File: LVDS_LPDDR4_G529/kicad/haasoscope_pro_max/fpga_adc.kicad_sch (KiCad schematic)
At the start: 2 parts, among them IC1 ADC12DL500ACF_Aligned, U3 Ti90G529_Functions

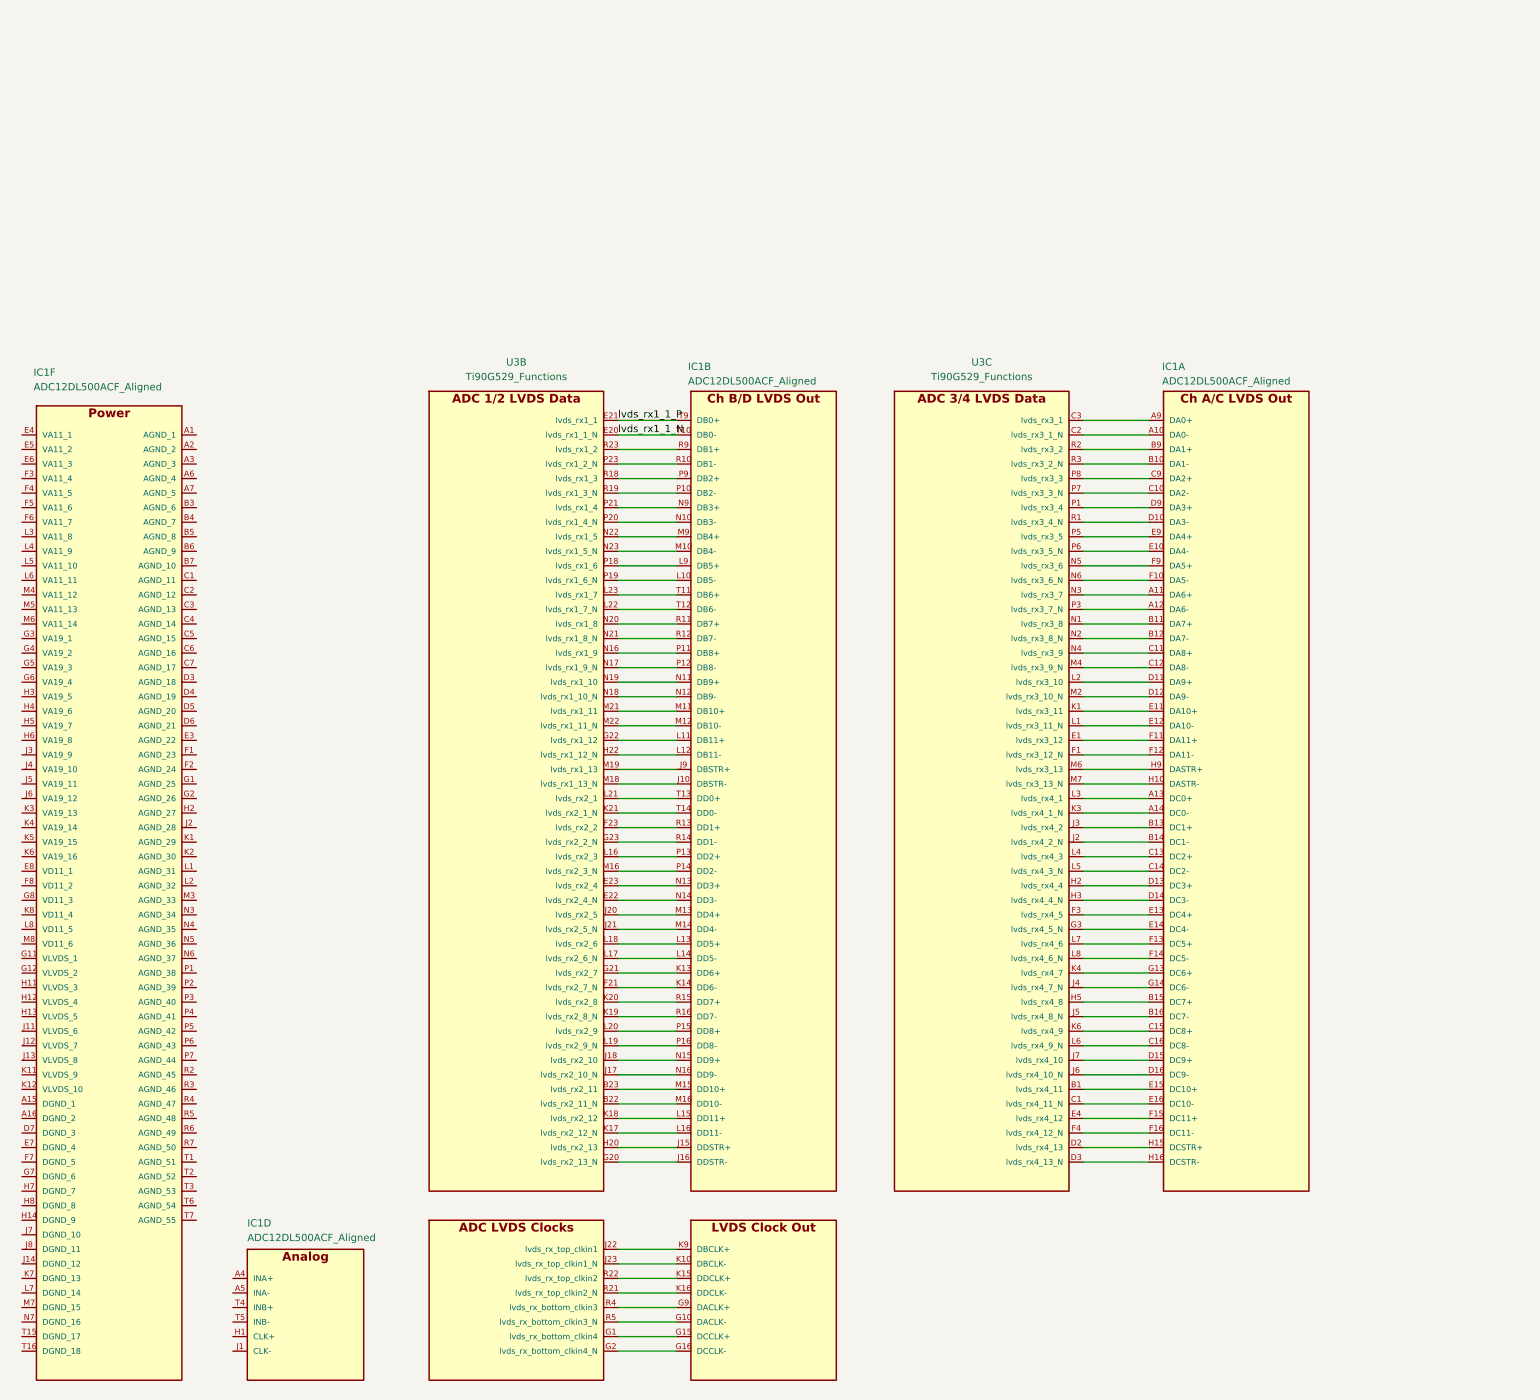
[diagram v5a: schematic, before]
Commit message: 6 NC pads
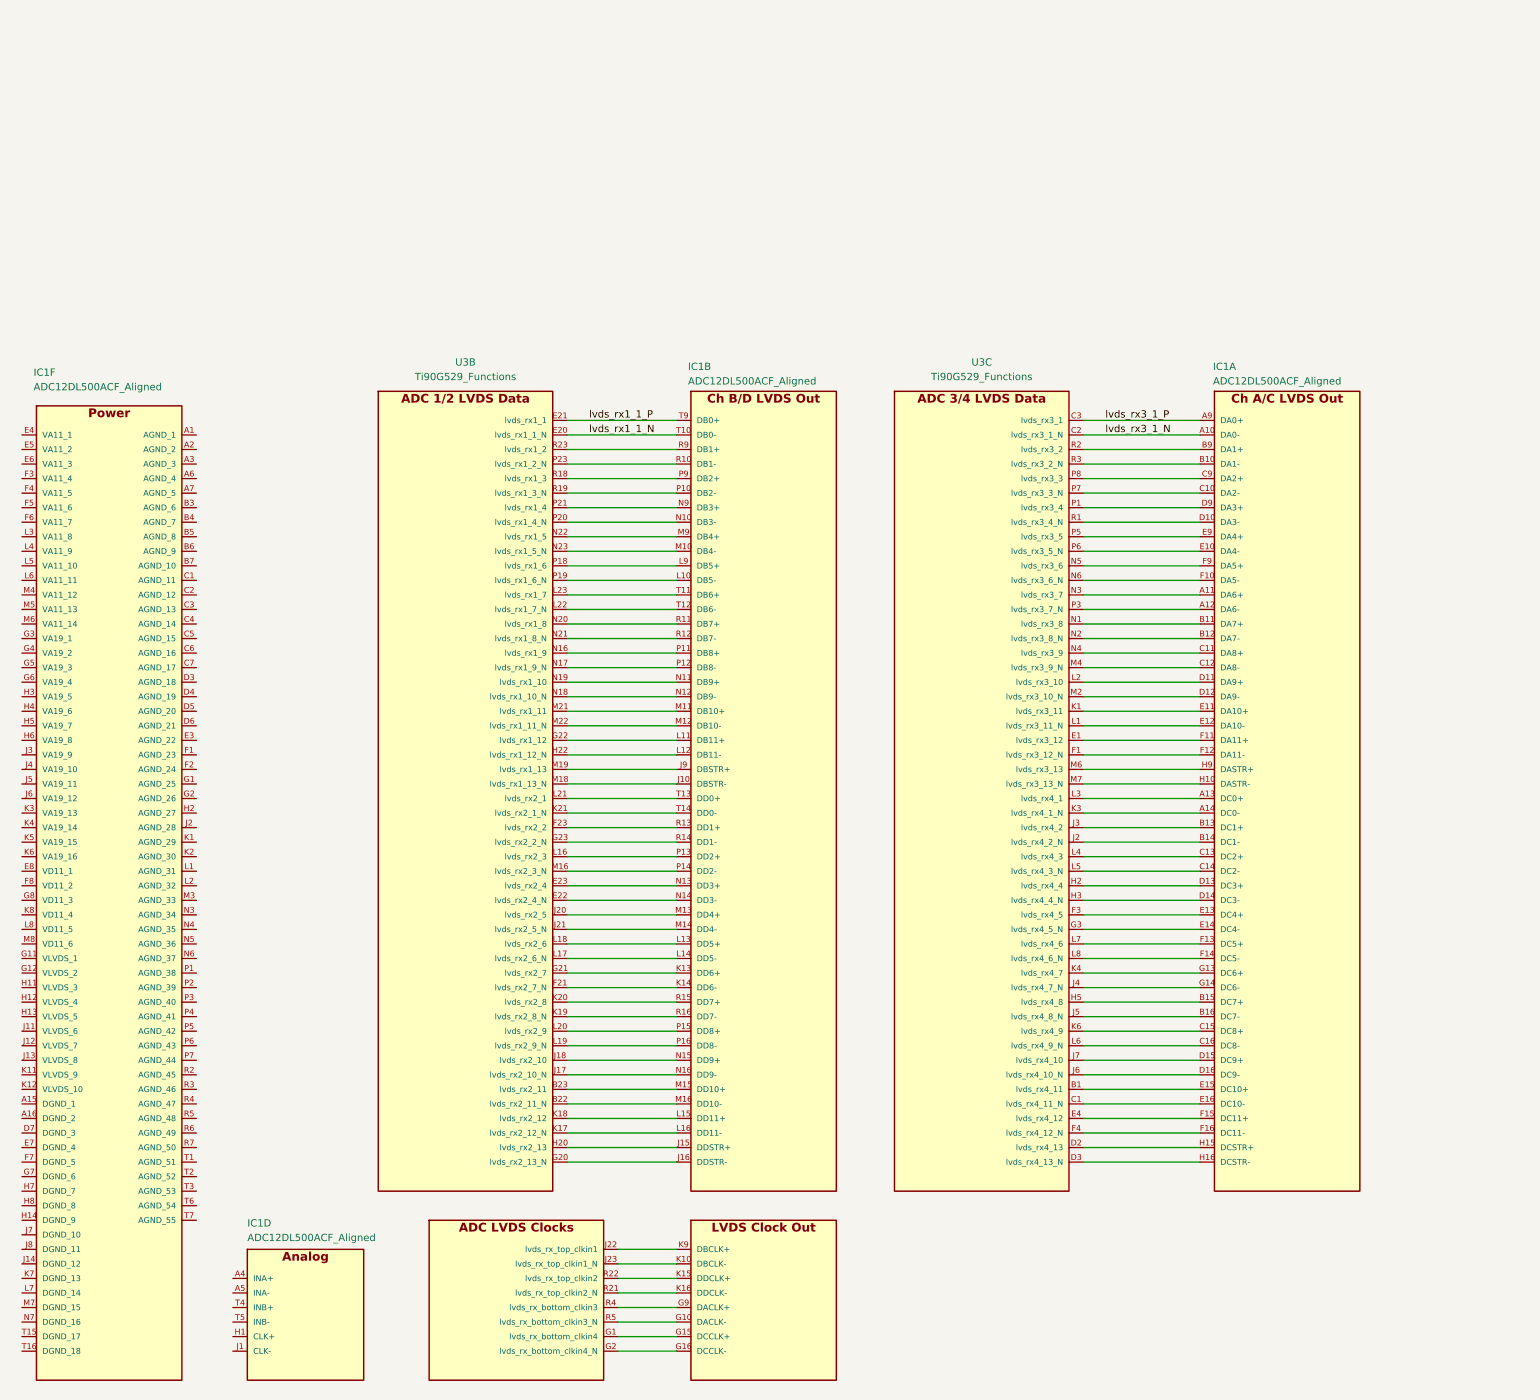
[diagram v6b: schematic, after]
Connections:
- net lvds_rx3_1_N: now reaches IC1.A10 (DA0-), U3.C2 (lvds_rx3_1_N)
- net lvds_rx3_1_P: now reaches IC1.A9 (DA0+), U3.C3 (lvds_rx3_1)
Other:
- moved on the sheet: IC1A, U3B

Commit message: add labels for all lvds_rx nets
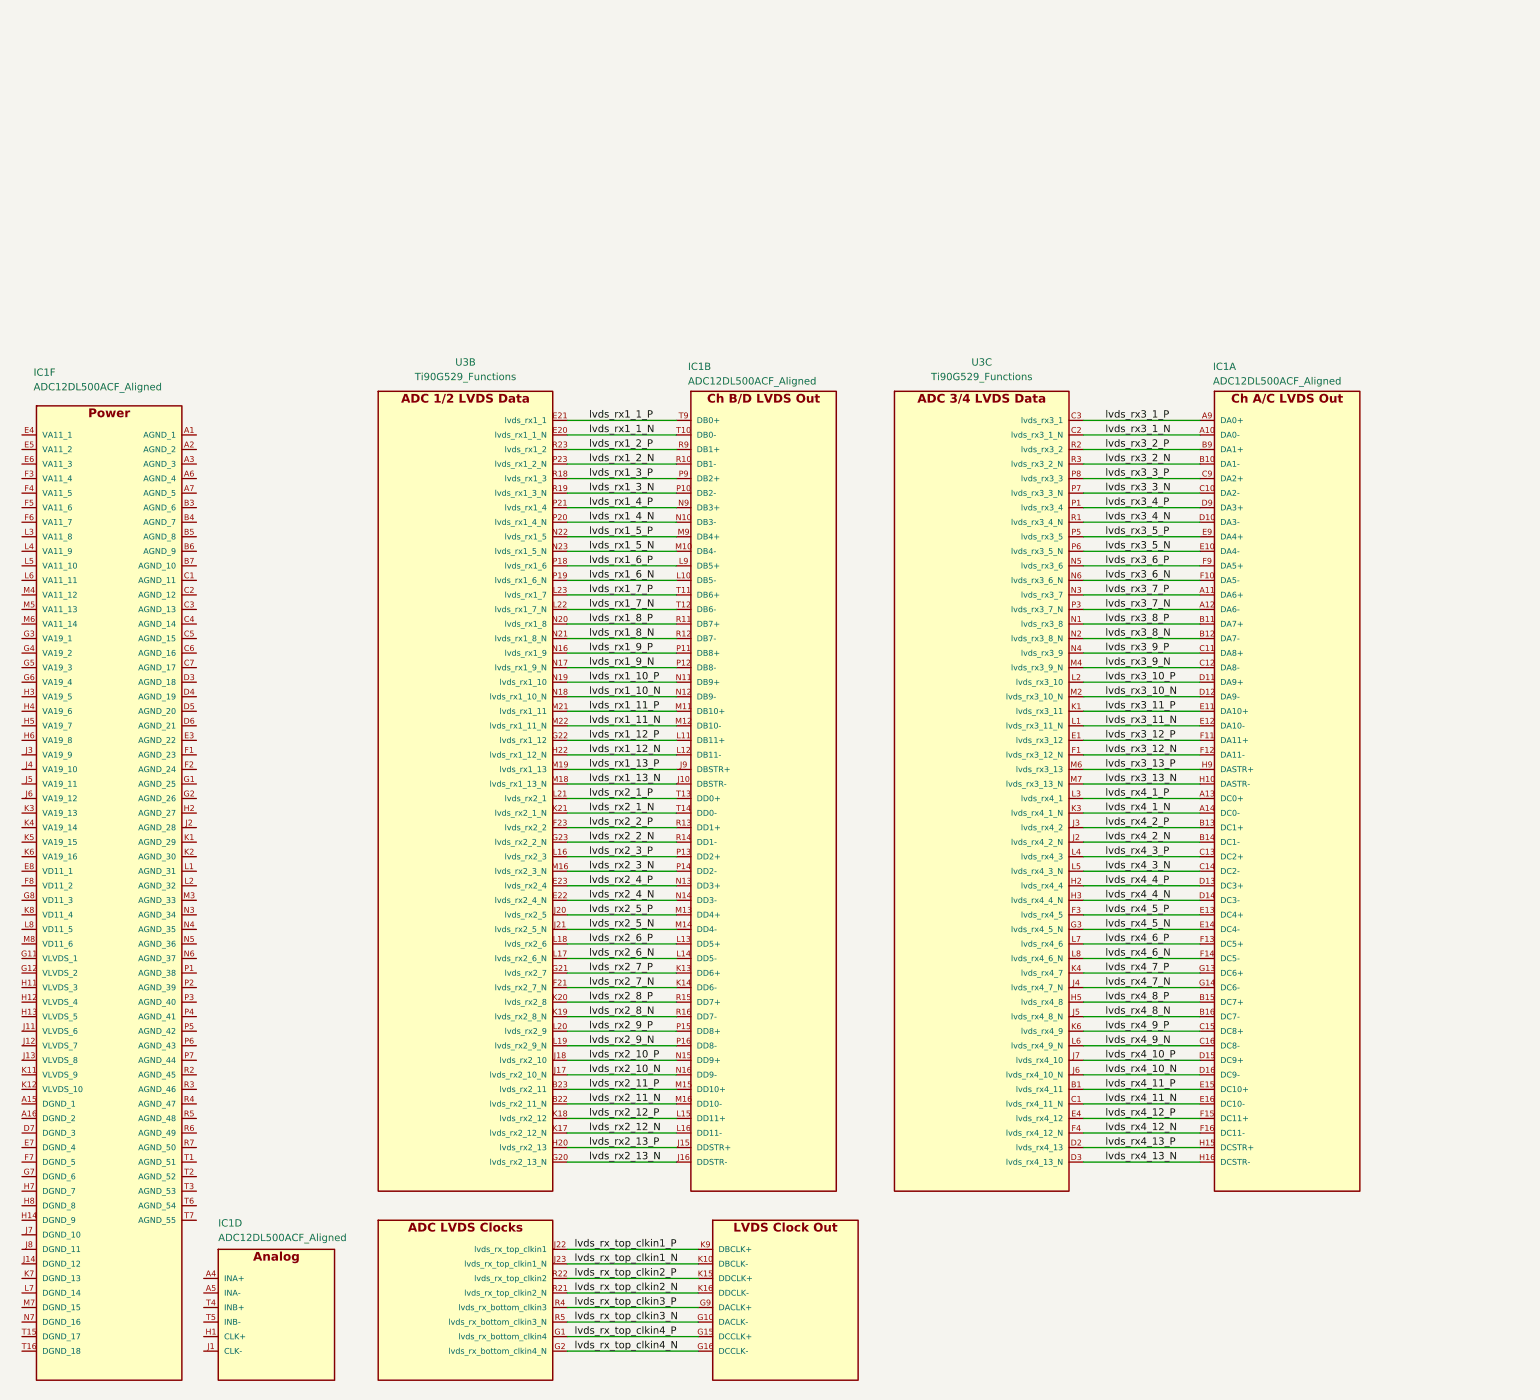
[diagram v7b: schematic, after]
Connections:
- net lvds_rx4_11_P: now reaches IC1.E15 (DC10+), U3.B1 (lvds_rx4_11)
- net lvds_rx4_11_N: now reaches IC1.E16 (DC10-), U3.C1 (lvds_rx4_11_N)
- net lvds_rx4_13_P: now reaches IC1.H15 (DCSTR+), U3.D2 (lvds_rx4_13)
- net lvds_rx4_13_N: now reaches IC1.H16 (DCSTR-), U3.D3 (lvds_rx4_13_N)
- net lvds_rx3_12_P: now reaches IC1.F11 (DA11+), U3.E1 (lvds_rx3_12)
- net lvds_rx4_12_P: now reaches IC1.F15 (DC11+), U3.E4 (lvds_rx4_12)
- net lvds_rx3_12_N: now reaches IC1.F12 (DA11-), U3.F1 (lvds_rx3_12_N)
- net lvds_rx4_5_P: now reaches IC1.E13 (DC4+), U3.F3 (lvds_rx4_5)
- net lvds_rx4_12_N: now reaches IC1.F16 (DC11-), U3.F4 (lvds_rx4_12_N)
- net lvds_rx4_5_N: now reaches IC1.E14 (DC4-), U3.G3 (lvds_rx4_5_N)
- net lvds_rx4_4_P: now reaches IC1.D13 (DC3+), U3.H2 (lvds_rx4_4)
- net lvds_rx4_4_N: now reaches IC1.D14 (DC3-), U3.H3 (lvds_rx4_4_N)
- net lvds_rx4_8_P: now reaches IC1.B15 (DC7+), U3.H5 (lvds_rx4_8)
- net lvds_rx4_2_N: now reaches IC1.B14 (DC1-), U3.J2 (lvds_rx4_2_N)
- net lvds_rx4_2_P: now reaches IC1.B13 (DC1+), U3.J3 (lvds_rx4_2)
- net lvds_rx4_7_N: now reaches IC1.G14 (DC6-), U3.J4 (lvds_rx4_7_N)
- net lvds_rx4_8_N: now reaches IC1.B16 (DC7-), U3.J5 (lvds_rx4_8_N)
- net lvds_rx4_10_N: now reaches IC1.D16 (DC9-), U3.J6 (lvds_rx4_10_N)
- net lvds_rx4_10_P: now reaches IC1.D15 (DC9+), U3.J7 (lvds_rx4_10)
- net lvds_rx3_11_P: now reaches IC1.E11 (DA10+), U3.K1 (lvds_rx3_11)
- net lvds_rx4_1_N: now reaches IC1.A14 (DC0-), U3.K3 (lvds_rx4_1_N)
- net lvds_rx4_7_P: now reaches IC1.G13 (DC6+), U3.K4 (lvds_rx4_7)
- net lvds_rx4_9_P: now reaches IC1.C15 (DC8+), U3.K6 (lvds_rx4_9)
- net lvds_rx3_11_N: now reaches IC1.E12 (DA10-), U3.L1 (lvds_rx3_11_N)
- net lvds_rx3_10_P: now reaches IC1.D11 (DA9+), U3.L2 (lvds_rx3_10)
- net lvds_rx4_1_P: now reaches IC1.A13 (DC0+), U3.L3 (lvds_rx4_1)
- net lvds_rx4_3_P: now reaches IC1.C13 (DC2+), U3.L4 (lvds_rx4_3)
- net lvds_rx4_3_N: now reaches IC1.C14 (DC2-), U3.L5 (lvds_rx4_3_N)
- net lvds_rx4_9_N: now reaches IC1.C16 (DC8-), U3.L6 (lvds_rx4_9_N)
- net lvds_rx4_6_P: now reaches IC1.F13 (DC5+), U3.L7 (lvds_rx4_6)
- net lvds_rx4_6_N: now reaches IC1.F14 (DC5-), U3.L8 (lvds_rx4_6_N)
- net lvds_rx3_10_N: now reaches IC1.D12 (DA9-), U3.M2 (lvds_rx3_10_N)
- net lvds_rx3_9_N: now reaches IC1.C12 (DA8-), U3.M4 (lvds_rx3_9_N)
- net lvds_rx3_13_P: now reaches IC1.H9 (DASTR+), U3.M6 (lvds_rx3_13)
- net lvds_rx3_13_N: now reaches IC1.H10 (DASTR-), U3.M7 (lvds_rx3_13_N)
- net lvds_rx3_8_P: now reaches IC1.B11 (DA7+), U3.N1 (lvds_rx3_8)
- net lvds_rx3_8_N: now reaches IC1.B12 (DA7-), U3.N2 (lvds_rx3_8_N)
- net lvds_rx3_7_P: now reaches IC1.A11 (DA6+), U3.N3 (lvds_rx3_7)
- net lvds_rx3_9_P: now reaches IC1.C11 (DA8+), U3.N4 (lvds_rx3_9)
- net lvds_rx3_6_P: now reaches IC1.F9 (DA5+), U3.N5 (lvds_rx3_6)
- net lvds_rx3_6_N: now reaches IC1.F10 (DA5-), U3.N6 (lvds_rx3_6_N)
- net lvds_rx3_4_P: now reaches IC1.D9 (DA3+), U3.P1 (lvds_rx3_4)
- net lvds_rx3_7_N: now reaches IC1.A12 (DA6-), U3.P3 (lvds_rx3_7_N)
- net lvds_rx3_5_P: now reaches IC1.E9 (DA4+), U3.P5 (lvds_rx3_5)
- net lvds_rx3_5_N: now reaches IC1.E10 (DA4-), U3.P6 (lvds_rx3_5_N)
- net lvds_rx3_3_N: now reaches IC1.C10 (DA2-), U3.P7 (lvds_rx3_3_N)
- net lvds_rx3_3_P: now reaches IC1.C9 (DA2+), U3.P8 (lvds_rx3_3)
- net lvds_rx3_4_N: now reaches IC1.D10 (DA3-), U3.R1 (lvds_rx3_4_N)
- net lvds_rx3_2_P: now reaches IC1.B9 (DA1+), U3.R2 (lvds_rx3_2)
- net lvds_rx3_2_N: now reaches IC1.B10 (DA1-), U3.R3 (lvds_rx3_2_N)
- net lvds_rx2_11_N: now reaches IC1.M16 (DD10-), U3.B22 (lvds_rx2_11_N)
- net lvds_rx2_11_P: now reaches IC1.M15 (DD10+), U3.B23 (lvds_rx2_11)
- net lvds_rx2_4_N: now reaches IC1.N14 (DD3-), U3.E22 (lvds_rx2_4_N)
- net lvds_rx2_4_P: now reaches IC1.N13 (DD3+), U3.E23 (lvds_rx2_4)
- net lvds_rx2_7_N: now reaches IC1.K14 (DD6-), U3.F21 (lvds_rx2_7_N)
- net lvds_rx2_2_P: now reaches IC1.R13 (DD1+), U3.F23 (lvds_rx2_2)
- net lvds_rx2_13_N: now reaches IC1.J16 (DDSTR-), U3.G20 (lvds_rx2_13_N)
- net lvds_rx2_7_P: now reaches IC1.K13 (DD6+), U3.G21 (lvds_rx2_7)
- net lvds_rx1_12_P: now reaches IC1.L11 (DB11+), U3.G22 (lvds_rx1_12)
- net lvds_rx2_2_N: now reaches IC1.R14 (DD1-), U3.G23 (lvds_rx2_2_N)
- net lvds_rx2_13_P: now reaches IC1.J15 (DDSTR+), U3.H20 (lvds_rx2_13)
- net lvds_rx1_12_N: now reaches IC1.L12 (DB11-), U3.H22 (lvds_rx1_12_N)
- net lvds_rx2_10_N: now reaches IC1.N16 (DD9-), U3.J17 (lvds_rx2_10_N)
- net lvds_rx2_10_P: now reaches IC1.N15 (DD9+), U3.J18 (lvds_rx2_10)
- net lvds_rx2_5_P: now reaches IC1.M13 (DD4+), U3.J20 (lvds_rx2_5)
- net lvds_rx2_5_N: now reaches IC1.M14 (DD4-), U3.J21 (lvds_rx2_5_N)
- net lvds_rx2_12_N: now reaches IC1.L16 (DD11-), U3.K17 (lvds_rx2_12_N)
- net lvds_rx2_12_P: now reaches IC1.L15 (DD11+), U3.K18 (lvds_rx2_12)
- net lvds_rx2_8_N: now reaches IC1.R16 (DD7-), U3.K19 (lvds_rx2_8_N)
- net lvds_rx2_8_P: now reaches IC1.R15 (DD7+), U3.K20 (lvds_rx2_8)
- net lvds_rx2_1_N: now reaches IC1.T14 (DD0-), U3.K21 (lvds_rx2_1_N)
- net lvds_rx2_3_P: now reaches IC1.P13 (DD2+), U3.L16 (lvds_rx2_3)
- net lvds_rx2_6_N: now reaches IC1.L14 (DD5-), U3.L17 (lvds_rx2_6_N)
- net lvds_rx2_6_P: now reaches IC1.L13 (DD5+), U3.L18 (lvds_rx2_6)
- net lvds_rx2_9_N: now reaches IC1.P16 (DD8-), U3.L19 (lvds_rx2_9_N)
- net lvds_rx2_9_P: now reaches IC1.P15 (DD8+), U3.L20 (lvds_rx2_9)
- net lvds_rx2_1_P: now reaches IC1.T13 (DD0+), U3.L21 (lvds_rx2_1)
- net lvds_rx1_7_N: now reaches IC1.T12 (DB6-), U3.L22 (lvds_rx1_7_N)
- net lvds_rx1_7_P: now reaches IC1.T11 (DB6+), U3.L23 (lvds_rx1_7)
- net lvds_rx2_3_N: now reaches IC1.P14 (DD2-), U3.M16 (lvds_rx2_3_N)
- net lvds_rx1_13_N: now reaches IC1.J10 (DBSTR-), U3.M18 (lvds_rx1_13_N)
- net lvds_rx1_13_P: now reaches IC1.J9 (DBSTR+), U3.M19 (lvds_rx1_13)
- net lvds_rx1_11_P: now reaches IC1.M11 (DB10+), U3.M21 (lvds_rx1_11)
- net lvds_rx1_11_N: now reaches IC1.M12 (DB10-), U3.M22 (lvds_rx1_11_N)
- net lvds_rx1_9_P: now reaches IC1.P11 (DB8+), U3.N16 (lvds_rx1_9)
- net lvds_rx1_9_N: now reaches IC1.P12 (DB8-), U3.N17 (lvds_rx1_9_N)
- net lvds_rx1_10_N: now reaches IC1.N12 (DB9-), U3.N18 (lvds_rx1_10_N)
- net lvds_rx1_10_P: now reaches IC1.N11 (DB9+), U3.N19 (lvds_rx1_10)
- net lvds_rx1_8_P: now reaches IC1.R11 (DB7+), U3.N20 (lvds_rx1_8)
- net lvds_rx1_8_N: now reaches IC1.R12 (DB7-), U3.N21 (lvds_rx1_8_N)
- net lvds_rx1_5_P: now reaches IC1.M9 (DB4+), U3.N22 (lvds_rx1_5)
- net lvds_rx1_5_N: now reaches IC1.M10 (DB4-), U3.N23 (lvds_rx1_5_N)
- net lvds_rx1_6_P: now reaches IC1.L9 (DB5+), U3.P18 (lvds_rx1_6)
- net lvds_rx1_6_N: now reaches IC1.L10 (DB5-), U3.P19 (lvds_rx1_6_N)
- net lvds_rx1_4_N: now reaches IC1.N10 (DB3-), U3.P20 (lvds_rx1_4_N)
- net lvds_rx1_4_P: now reaches IC1.N9 (DB3+), U3.P21 (lvds_rx1_4)
- net lvds_rx1_2_N: now reaches IC1.R10 (DB1-), U3.P23 (lvds_rx1_2_N)
- net lvds_rx1_3_P: now reaches IC1.P9 (DB2+), U3.R18 (lvds_rx1_3)
- net lvds_rx1_3_N: now reaches IC1.P10 (DB2-), U3.R19 (lvds_rx1_3_N)
- net lvds_rx1_2_P: now reaches IC1.R9 (DB1+), U3.R23 (lvds_rx1_2)
- net lvds_rx_top_clkin4_P: now reaches IC1.G15 (DCCLK+), U3.G1 (lvds_rx_bottom_clkin4)
- net lvds_rx_top_clkin4_N: now reaches IC1.G16 (DCCLK-), U3.G2 (lvds_rx_bottom_clkin4_N)
- net lvds_rx_top_clkin1_P: now reaches IC1.K9 (DBCLK+), U3.J22 (lvds_rx_top_clkin1)
- net lvds_rx_top_clkin1_N: now reaches IC1.K10 (DBCLK-), U3.J23 (lvds_rx_top_clkin1_N)
- net lvds_rx_top_clkin2_N: now reaches IC1.K16 (DDCLK-), U3.R21 (lvds_rx_top_clkin2_N)
- net lvds_rx_top_clkin2_P: now reaches IC1.K15 (DDCLK+), U3.R22 (lvds_rx_top_clkin2)
- net lvds_rx_top_clkin3_P: now reaches IC1.G9 (DACLK+), U3.R4 (lvds_rx_bottom_clkin3)
- net lvds_rx_top_clkin3_N: now reaches IC1.G10 (DACLK-), U3.R5 (lvds_rx_bottom_clkin3_N)
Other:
- moved on the sheet: IC1D
